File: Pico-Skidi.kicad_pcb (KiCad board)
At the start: 2 copper layers, 1 part, among them U4 Pico

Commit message: syncing
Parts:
- added C1: 10uf, Capacitor_SMD:C_0603_1608Metric_Pad1.08x0.95mm_HandSolder, F.Cu at (144.7, 35.5)
- added C2: 0.1uF, Capacitor_SMD:C_0603_1608Metric_Pad1.08x0.95mm_HandSolder, F.Cu at (148.1, 35.5)
- added C3: C, Capacitor_SMD:C_0603_1608Metric_Pad1.08x0.95mm_HandSolder, F.Cu at (151.4, 35.5)
- added C4: C, Capacitor_SMD:C_0603_1608Metric_Pad1.08x0.95mm_HandSolder, F.Cu at (144.7, 40.0)
- added C5: C, Capacitor_SMD:C_0603_1608Metric_Pad1.08x0.95mm_HandSolder, F.Cu at (148.1, 40.0)
- added C6: C, Capacitor_SMD:C_0603_1608Metric_Pad1.08x0.95mm_HandSolder, F.Cu at (151.4, 40.0)
- added C7: C, Capacitor_SMD:C_0603_1608Metric_Pad1.08x0.95mm_HandSolder, F.Cu at (144.7, 44.6)
- added D1: LED, LED_SMD:LED_0603_1608Metric_Pad1.05x0.95mm_HandSolder, F.Cu at (176.0, 41.5)
- added D2: LED, LED_SMD:LED_0603_1608Metric_Pad1.05x0.95mm_HandSolder, F.Cu at (180.4, 41.6)
- added J1: USB_C_Receptacle, Connector_USB:USB_C_Plug_Molex_105444, F.Cu at (216.1, 37.6)
- added J2: BAT, Connector_JST:JST_PH_S2B-PH-K_1x02_P2.00mm_Horizontal, F.Cu at (180.0, 80.0)
- added J3: Motor 3, Connector_PinHeader_2.54mm:PinHeader_1x02_P2.54mm_Vertical, F.Cu at (205.9, 81.5)
- added J4: Motor 4, Connector_PinHeader_2.54mm:PinHeader_1x02_P2.54mm_Vertical, F.Cu at (205.9, 85.1)
- added J5: Motor 1, Connector_PinHeader_2.54mm:PinHeader_1x02_P2.54mm_Vertical, F.Cu at (205.9, 74.2)
- added J6: Motor 2, Connector_PinHeader_2.54mm:PinHeader_1x02_P2.54mm_Vertical, F.Cu at (205.9, 77.9)
- added J7: Conn_01x03, Connector_PinHeader_2.54mm:PinHeader_1x03_P2.54mm_Vertical, F.Cu at (174.6, 88.1)
- added J8: Conn_01x04, Connector_PinHeader_2.54mm:PinHeader_1x04_P2.54mm_Vertical, F.Cu at (210.9, 92.4)
- added J9: RGBLED, Connector_PinHeader_2.54mm:PinHeader_1x03_P2.54mm_Vertical, F.Cu at (203.3, 88.8)
- added LS1: PKLCS1212E4001-R1, PKLCS1212:PKLCS_472x472_MUR, F.Cu at (151.5, 85.8)
- added M1: Motor_Servo, Connector_PinHeader_2.54mm:PinHeader_1x03_P2.54mm_Vertical, F.Cu at (203.3, 52.3)
- added M2: Motor_Servo, Connector_PinHeader_2.54mm:PinHeader_1x03_P2.54mm_Vertical, F.Cu at (203.3, 55.9)
- added M3: Motor_Servo, Connector_PinHeader_2.54mm:PinHeader_1x03_P2.54mm_Vertical, F.Cu at (203.3, 59.6)
- added M4: Motor_Servo, Connector_PinHeader_2.54mm:PinHeader_1x03_P2.54mm_Vertical, F.Cu at (203.3, 63.2)
- added M5: Motor_Servo, Connector_PinHeader_2.54mm:PinHeader_1x03_P2.54mm_Vertical, F.Cu at (203.3, 66.9)
- added M6: Motor_Servo, Connector_PinHeader_2.54mm:PinHeader_1x03_P2.54mm_Vertical, F.Cu at (203.3, 70.5)
- added Q1: Q_PMOS_GDS, Connector_PinHeader_2.54mm:PinHeader_1x03_P2.54mm_Vertical, F.Cu at (168.1, 67.3)
- added Q2: Q_NMOS_DGS, Connector_PinHeader_2.54mm:PinHeader_1x03_P2.54mm_Vertical, F.Cu at (172.8, 67.3)
- added Q3: Q_NMOS_DGS, Connector_PinHeader_2.54mm:PinHeader_1x03_P2.54mm_Vertical, F.Cu at (177.4, 67.3)
- added R1: 5k1, Resistor_SMD:R_0603_1608Metric_Pad0.98x0.95mm_HandSolder, F.Cu at (162.1, 33.9)
- added R10: R, Resistor_SMD:R_0603_1608Metric_Pad0.98x0.95mm_HandSolder, F.Cu at (162.1, 47.6)
- added R11: R, Resistor_SMD:R_0603_1608Metric_Pad0.98x0.95mm_HandSolder, F.Cu at (165.5, 47.6)
- added R12: R, Resistor_SMD:R_0603_1608Metric_Pad0.98x0.95mm_HandSolder, F.Cu at (168.8, 47.6)
- added R2: 5k1, Resistor_SMD:R_0603_1608Metric_Pad0.98x0.95mm_HandSolder, F.Cu at (165.5, 33.9)
- added R3: 2k, Resistor_SMD:R_0603_1608Metric_Pad0.98x0.95mm_HandSolder, F.Cu at (168.8, 33.9)
- added R4: 2k, Resistor_SMD:R_0603_1608Metric_Pad0.98x0.95mm_HandSolder, F.Cu at (162.1, 38.5)
- added R5: 4k99, Resistor_SMD:R_0603_1608Metric_Pad0.98x0.95mm_HandSolder, F.Cu at (165.5, 38.5)
- added R6: 3k3, Resistor_SMD:R_0603_1608Metric_Pad0.98x0.95mm_HandSolder, F.Cu at (168.8, 38.5)
- added R7: 330, Resistor_SMD:R_0603_1608Metric_Pad0.98x0.95mm_HandSolder, F.Cu at (162.1, 43.0)
- added R8: 2.2k, Resistor_SMD:R_0603_1608Metric_Pad0.98x0.95mm_HandSolder, F.Cu at (165.5, 43.0)
- added R9: R, Resistor_SMD:R_0603_1608Metric_Pad0.98x0.95mm_HandSolder, F.Cu at (168.8, 43.0)
- added U1: MCP73831T-2ACI/OT, MCP73831:SOT-23-5_MC_MCH, F.Cu at (185.9, 54.8)
- added U2: BQ29700DSER, BQ29700DSER:DSE0006A, F.Cu at (187.1, 34.8)
- added U3: PDRV8411PWPR, DRV8411:TSSOP_11PWPR_TEX, F.Cu at (121.9, 45.5)
- added U5: Pico, MCU_RaspberryPi_and_Boards:RPi_Pico_W_SMD, F.Cu at (220.4, 103.4)
- U4: value Pico -> PDRV8411PWPR; footprint MCU_RaspberryPi_and_Boards:RPi_Pico_W_SMD_TH -> DRV8411:TSSOP_11PWPR_TEX
- moved U4 62.7 mm to (104.8, 45.9)
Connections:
- U4 pad 1: unconnected-(U4-GPIO0-Pad1) -> Net-(U4-AISEN)
- U4 pad 10: /Motor Management/MOT_A- -> +5V
- U4 pad 11: /Pico W/SRV_05 -> GND
- U4 pad 12: /Pico W/SRV_06 -> unconnected-(U4-NC-Pad12)
- U4 pad 13: GND -> /Motor Management/MOT_C-
- U4 pad 14: /Motor Management/nFAULT_01 -> /Motor Management/MOT_C+
- U4 pad 15: /Motor Management/nFAULT_02 -> unconnected-(U4-nSLEEP-Pad15)
- U4 pad 16: /Motor Management/MOT_C+ -> Net-(J3-Pin_1)
- U4 pad 2: unconnected-(U4-GPIO1-Pad2) -> Net-(J3-Pin_2)
- U4 pad 3: GND -> Net-(J4-Pin_2)
- U4 pad 4: /Pico W/SRV_01 -> Net-(U4-BISEN)
- U4 pad 5: /Pico W/SRV_02 -> Net-(J4-Pin_1)
- U4 pad 6: /Pico W/SRV_03 -> /Motor Management/nFAULT_02
- U4 pad 7: /Pico W/SRV_04 -> /Motor Management/MOT_D+
- U4 pad 8: GND -> /Motor Management/MOT_D-
- U4 pad 9: /Motor Management/MOT_A+ -> unconnected-(U4-NC-Pad9)
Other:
- board outline added: 42 x 54 mm

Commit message: progress at last
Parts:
- removed C1: 10uf, Capacitor_SMD:C_0603_1608Metric_Pad1.08x0.95mm_HandSolder
- removed C2: 0.1uF, Capacitor_SMD:C_0603_1608Metric_Pad1.08x0.95mm_HandSolder
- removed C3: C, Capacitor_SMD:C_0603_1608Metric_Pad1.08x0.95mm_HandSolder
- removed D1, D2: LED, LED_SMD:LED_0603_1608Metric_Pad1.05x0.95mm_HandSolder
- removed J1: USB_C_Receptacle, Connector_USB:USB_C_Plug_Molex_105444
- removed J2: BAT, Connector_JST:JST_PH_S2B-PH-K_1x02_P2.00mm_Horizontal
- removed J7: Conn_01x03, Connector_PinHeader_2.54mm:PinHeader_1x03_P2.54mm_Vertical
- removed Q1: Q_PMOS_GDS, Connector_PinHeader_2.54mm:PinHeader_1x03_P2.54mm_Vertical
- removed Q2, Q3: Q_NMOS_DGS, Connector_PinHeader_2.54mm:PinHeader_1x03_P2.54mm_Vertical
- removed R1, R2: 5k1, Resistor_SMD:R_0603_1608Metric_Pad0.98x0.95mm_HandSolder
- removed R3, R4: 2k, Resistor_SMD:R_0603_1608Metric_Pad0.98x0.95mm_HandSolder
- removed R5: 4k99, Resistor_SMD:R_0603_1608Metric_Pad0.98x0.95mm_HandSolder
- removed R6: 3k3, Resistor_SMD:R_0603_1608Metric_Pad0.98x0.95mm_HandSolder
- removed R7: 330, Resistor_SMD:R_0603_1608Metric_Pad0.98x0.95mm_HandSolder
- removed R8: 2.2k, Resistor_SMD:R_0603_1608Metric_Pad0.98x0.95mm_HandSolder
- removed U1: MCP73831T-2ACI/OT, MCP73831:SOT-23-5_MC_MCH
- removed U2: BQ29700DSER, BQ29700DSER:DSE0006A
- U5: footprint MCU_RaspberryPi_and_Boards:RPi_Pico_W_SMD -> pico-skidi:RPi_Pico_TH
- moved U4 113.8 mm to (213.4, 79.8), turned to 90 degrees
- moved U3 103.5 mm to (210.3, 99.5)
- moved C7 92.4 mm to (216.4, 102.9)
- moved C5 91.8 mm to (216.4, 101.4)
- moved LS1 79.8 mm to (230.8, 94.8)
- moved C4 78.8 mm to (216.1, 73.4)
- moved C6 73.5 mm to (216.1, 74.9)
- moved R10 66.3 mm to (208.3, 95.1)
- moved R12 62.6 mm to (204.6, 98.9), turned to 180 degrees
- moved R11 60.8 mm to (213.1, 85.5), turned to -90 degrees
- moved R9 56.5 mm to (209.8, 81.9), turned to 90 degrees
- moved U5 29.4 mm to (231.0, 76.0)
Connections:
- U5 pad 39: +5V -> VSYS
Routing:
- net +5V: track 0.00 -> 82.9 mm, vias 0 -> 2
- net /Motor Management/MOT_B+: track 0.00 -> 65.5 mm, vias 0 -> 1
- net /Motor Management/MOT_B-: track 0.00 -> 63.6 mm, vias 0 -> 1
- net +3.3V: track 0.00 -> 57.4 mm
- net /Motor Management/nFAULT_01: track 0.00 -> 50.4 mm, vias 0 -> 1
- net /Motor Management/MOT_A+: track 0.00 -> 47.3 mm, vias 0 -> 1
- net Net-(J5-Pin_1): track 0.00 -> 43.8 mm, vias 0 -> 2
- net /Pico W/SRV_06: track 0.00 -> 43.5 mm, vias 0 -> 1
- net /Motor Management/MOT_A-: track 0.00 -> 42.3 mm, vias 0 -> 1
- net /Pico W/SCL: track 0.00 -> 42.3 mm
- net /Pico W/SDA: track 0.00 -> 40.5 mm, vias 0 -> 2
- net /Extras/RGB_LED: track 0.00 -> 37.0 mm, vias 0 -> 2
- net Net-(J6-Pin_1): track 0.00 -> 32.6 mm, vias 0 -> 1
- net /Motor Management/MOT_C+: track 0.00 -> 30.6 mm, vias 0 -> 2
- net Net-(J5-Pin_2): track 0.00 -> 30.4 mm, vias 0 -> 2
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- added copper zone on B.Cu, net GND
- added copper zone on F.Cu, net GND

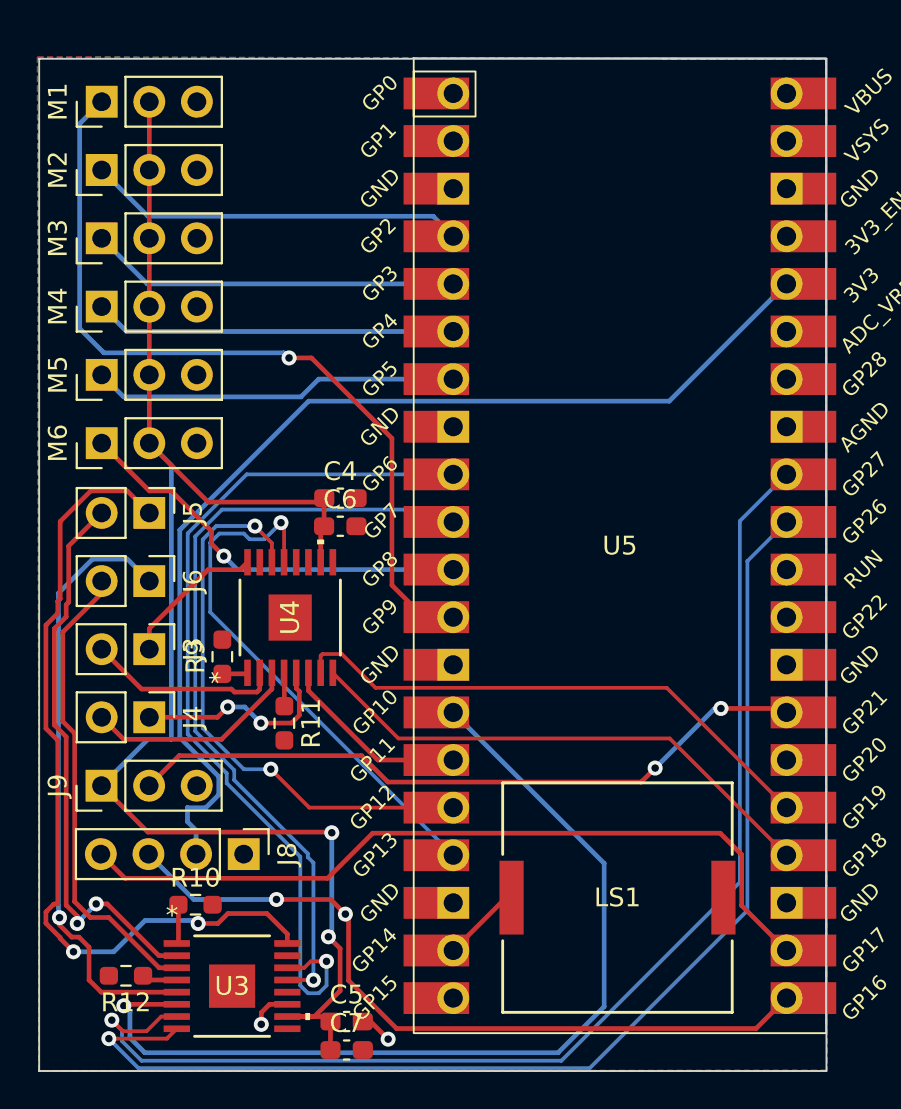
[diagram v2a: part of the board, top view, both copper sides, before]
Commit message: Adding Power
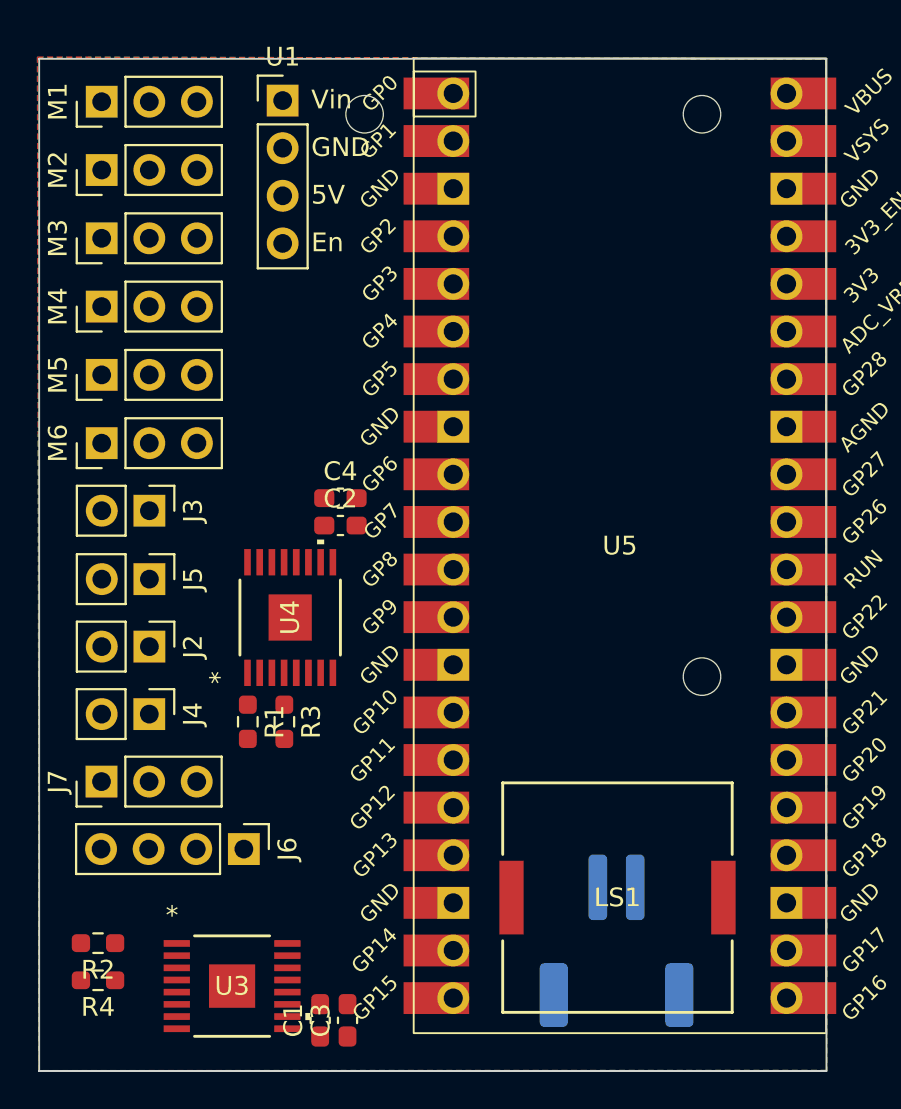
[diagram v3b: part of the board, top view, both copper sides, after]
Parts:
- removed C5, C6, C7: C, Capacitor_SMD:C_0603_1608Metric_Pad1.08x0.95mm_HandSolder
- removed J8: Conn_01x04, Connector_PinHeader_2.54mm:PinHeader_1x04_P2.54mm_Vertical
- removed J9: RGBLED, Connector_PinHeader_2.54mm:PinHeader_1x03_P2.54mm_Vertical
- removed R10, R11, R12, R9: R, Resistor_SMD:R_0603_1608Metric_Pad0.98x0.95mm_HandSolder
- added C1: C, Capacitor_SMD:C_0603_1608Metric_Pad1.08x0.95mm_HandSolder, F.Cu at (215.0, 101.3)
- added C2: C, Capacitor_SMD:C_0603_1608Metric_Pad1.08x0.95mm_HandSolder, F.Cu at (216.1, 74.9)
- added C3: C, Capacitor_SMD:C_0603_1608Metric_Pad1.08x0.95mm_HandSolder, F.Cu at (216.4, 101.3)
- added J1: Conn_01x02, Connector_JST:JST_PH_S2B-PH-SM4-TB_1x02-1MP_P2.00mm_Horizontal, B.Cu at (230.8, 97.0)
- added J2: Motor 3, Connector_PinHeader_2.54mm:PinHeader_1x02_P2.54mm_Vertical, F.Cu at (205.9, 81.4)
- added J7: RGBLED, Connector_PinHeader_2.54mm:PinHeader_1x03_P2.54mm_Vertical, F.Cu at (203.3, 88.6)
- added R1: R, Resistor_SMD:R_0603_1608Metric_Pad0.98x0.95mm_HandSolder, F.Cu at (211.1, 85.4)
- added R2: R, Resistor_SMD:R_0603_1608Metric_Pad0.98x0.95mm_HandSolder, F.Cu at (203.1, 97.2)
- added R3: R, Resistor_SMD:R_0603_1608Metric_Pad0.98x0.95mm_HandSolder, F.Cu at (213.1, 85.4)
- added R4: R, Resistor_SMD:R_0603_1608Metric_Pad0.98x0.95mm_HandSolder, F.Cu at (203.1, 99.2)
- added U1: ~, pico-skidi:TPS61023, F.Cu at (213.0, 52.2)
- added U2: ~, pico-skidi:Pimoroni Amigo Pro Mounts, B.Cu at (237.9, 50.5)
- J3: value Motor 3 -> Motor 4
- J4: value Motor 4 -> Motor 1
- J5: value Motor 1 -> Motor 2
- J6: value Motor 2 -> Conn_01x04; footprint Connector_PinHeader_2.54mm:PinHeader_1x02_P2.54mm_Vertical -> Connector_PinHeader_2.54mm:PinHeader_1x04_P2.54mm_Vertical
- moved J6 15.2 mm to (210.9, 92.2)
- moved J3 7.39 mm to (205.9, 74.1)
- moved J5 3.53 mm to (205.9, 77.8)
- moved J4 0.17 mm to (205.9, 85.0)
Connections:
- J6 pad 1: Net-(J6-Pin_1) -> GND
- J6 pad 2: Net-(J6-Pin_2) -> +3.3V
- U3 pad 16: Net-(J5-Pin_1) -> Net-(J4-Pin_1)
- U3 pad 2: Net-(J5-Pin_2) -> Net-(J4-Pin_2)
- U3 pad 3: Net-(J6-Pin_2) -> Net-(J5-Pin_2)
- U3 pad 5: Net-(J6-Pin_1) -> Net-(J5-Pin_1)
- U4 pad 16: Net-(J3-Pin_1) -> Net-(J2-Pin_1)
- U4 pad 2: Net-(J3-Pin_2) -> Net-(J2-Pin_2)
- U4 pad 3: Net-(J4-Pin_2) -> Net-(J3-Pin_2)
- U4 pad 5: Net-(J4-Pin_1) -> Net-(J3-Pin_1)
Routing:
- net +5V: track 82.9 -> 0.00 mm, vias 2 -> 0
- net /Motor Management/MOT_B+: track 65.5 -> 0.00 mm, vias 1 -> 0
- net /Motor Management/MOT_B-: track 63.6 -> 0.00 mm, vias 1 -> 0
- net +3.3V: track 57.4 -> 0.00 mm
- net /Motor Management/nFAULT_01: track 50.4 -> 0.00 mm, vias 1 -> 0
- net /Motor Management/MOT_A+: track 47.3 -> 0.00 mm, vias 1 -> 0
- net Net-(J5-Pin_1): track 43.8 -> 0.00 mm, vias 2 -> 0
- net /Pico W/SRV_06: track 43.5 -> 0.00 mm, vias 1 -> 0
- net /Motor Management/MOT_A-: track 42.3 -> 0.00 mm, vias 1 -> 0
- net /Pico W/SCL: track 42.3 -> 0.00 mm
- net /Pico W/SDA: track 40.5 -> 0.00 mm, vias 2 -> 0
- net /Extras/RGB_LED: track 37.0 -> 0.00 mm, vias 2 -> 0
- net Net-(J6-Pin_1): track 32.6 -> 0.00 mm, vias 1 -> 0
- net /Motor Management/MOT_C+: track 30.6 -> 0.00 mm, vias 2 -> 0
- net Net-(J5-Pin_2): track 30.4 -> 0.00 mm, vias 2 -> 0
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
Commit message: Routed, now just silk screens left
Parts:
- moved R4 0.54 mm to (203.1, 99.7)
- moved C1 0.54 mm to (215.0, 100.8)
- moved C3 0.54 mm to (216.4, 100.8)
- moved R3 0.47 mm to (213.3, 85.8)
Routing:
- net VSYS: track 0.00 -> 133.4 mm, vias 0 -> 4
- net +5V: track 0.00 -> 100.3 mm, vias 0 -> 2
- net /Motor Management/MOT_B+: track 0.00 -> 64.8 mm, vias 0 -> 1
- net /Motor Management/MOT_B-: track 0.00 -> 58.2 mm, vias 0 -> 1
- net GND: track 0.00 -> 55.3 mm, vias 0 -> 22
- net +3.3V: track 0.00 -> 53.2 mm, vias 0 -> 2
- net /Motor Management/MOT_A-: track 0.00 -> 52.2 mm
- net /Motor Management/nFAULT_01: track 0.00 -> 51.2 mm
- net /Pico W/SCL: track 0.00 -> 45.2 mm, vias 0 -> 1
- net /Pico W/SDA: track 0.00 -> 40.9 mm, vias 0 -> 1
- net /Pico W/SRV_06: track 0.00 -> 39.1 mm, vias 0 -> 2
- net /Extras/RGB_LED: track 0.00 -> 37.3 mm, vias 0 -> 3
- net Net-(J5-Pin_1): track 0.00 -> 35.7 mm
- net /Motor Management/MOT_A+: track 0.00 -> 32.8 mm
- net /Motor Management/MOT_D+: track 0.00 -> 31.6 mm, vias 0 -> 1
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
